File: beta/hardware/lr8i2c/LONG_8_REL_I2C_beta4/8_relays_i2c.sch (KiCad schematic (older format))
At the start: 86 parts, among them K101 G5LA-1-12VDC, K102 G5LA-1-12VDC, K103 G5LA-1-12VDC, K104 G5LA-1-12VDC, K105 G5LA-1-12VDC, K106 G5LA-1-12VDC, K107 G5LA-1-12VDC, K108 G5LA-1-12VDC, P101 CONN_3, P102 CONN_3, P103 CONN_3, P104 CONN_3, P105 CONN_3, P106 CONN_3, P107 CONN_3, P108 CONN_3, P109 CONN_2, P110 CONN_6, P112 CONN_6, Q101 PNP, Q102 PNP, Q103 PNP, Q104 PNP, Q105 PNP, Q106 PNP, Q107 PNP, Q108 PNP, Q109 DSS20201L NPN, Q110 DSS20201L NPN, Q111 DSS20201L NPN, Q112 DSS20201L NPN, Q113 DSS20201L NPN, Q114 DSS20201L NPN, Q115 DSS20201L NPN, Q116 DSS20201L NPN, U101 PCF8574P

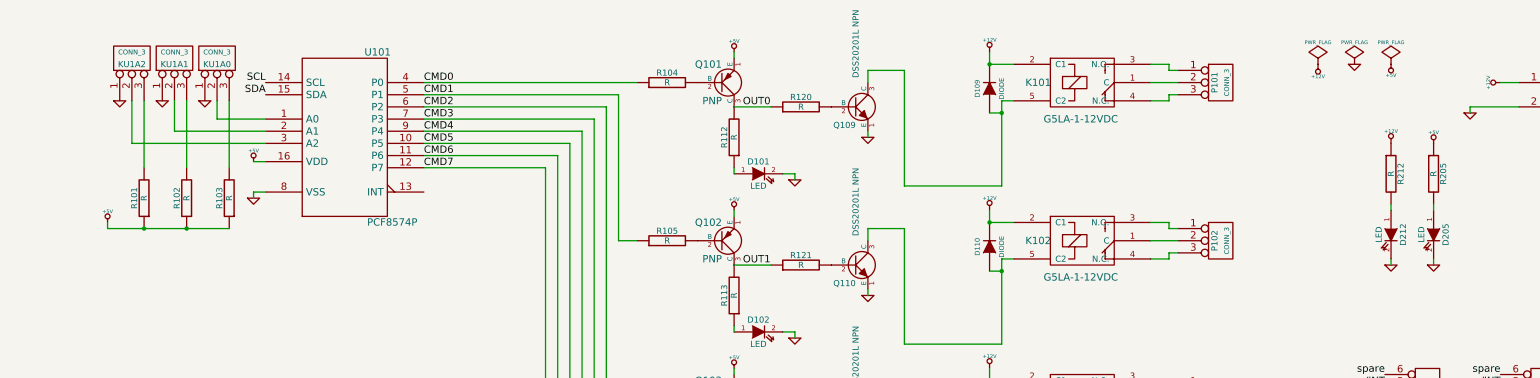
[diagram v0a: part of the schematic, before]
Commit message: Suppression 2 des 3 resistances de pull-up d'adressage Ajout pre-disposition 2 resistance de pull-up SDA/SCL Controle DRC ok
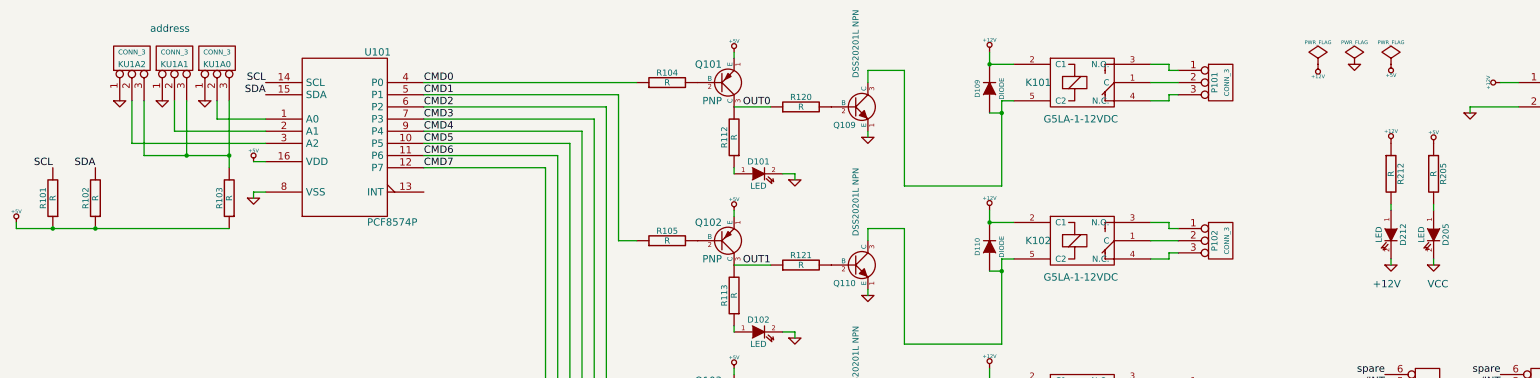
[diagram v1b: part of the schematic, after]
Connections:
- net SCL: now also R101.2
- net SDA: now also R102.2
- net at KU1A2.3 (P3): now also KU1A0.3 (P3), KU1A1.3 (P3), R103.2; no longer R101.2
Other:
- note added: "+12V"
- note added: "VCC"
- note added: "address"
- moved on the sheet: R101, R102

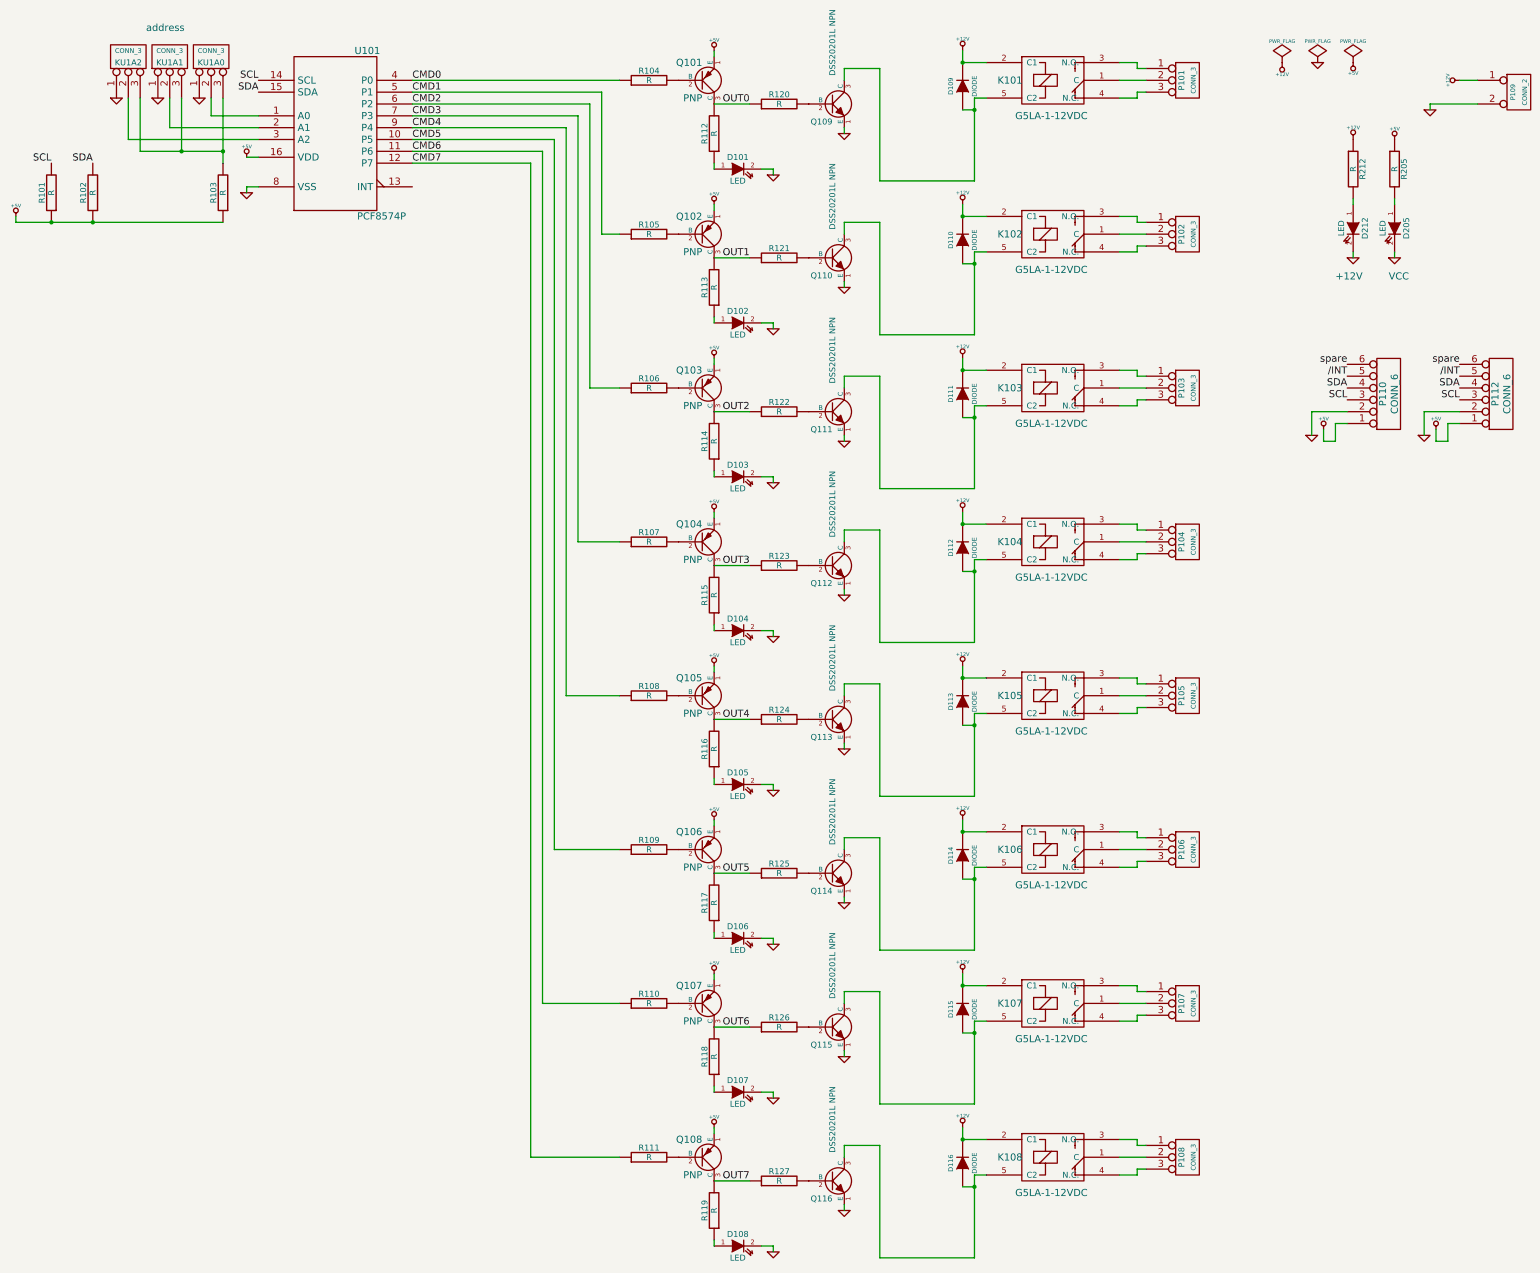
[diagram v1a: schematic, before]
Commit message: ajout d'un second connecteur GND-12V ajout logos DRC ok
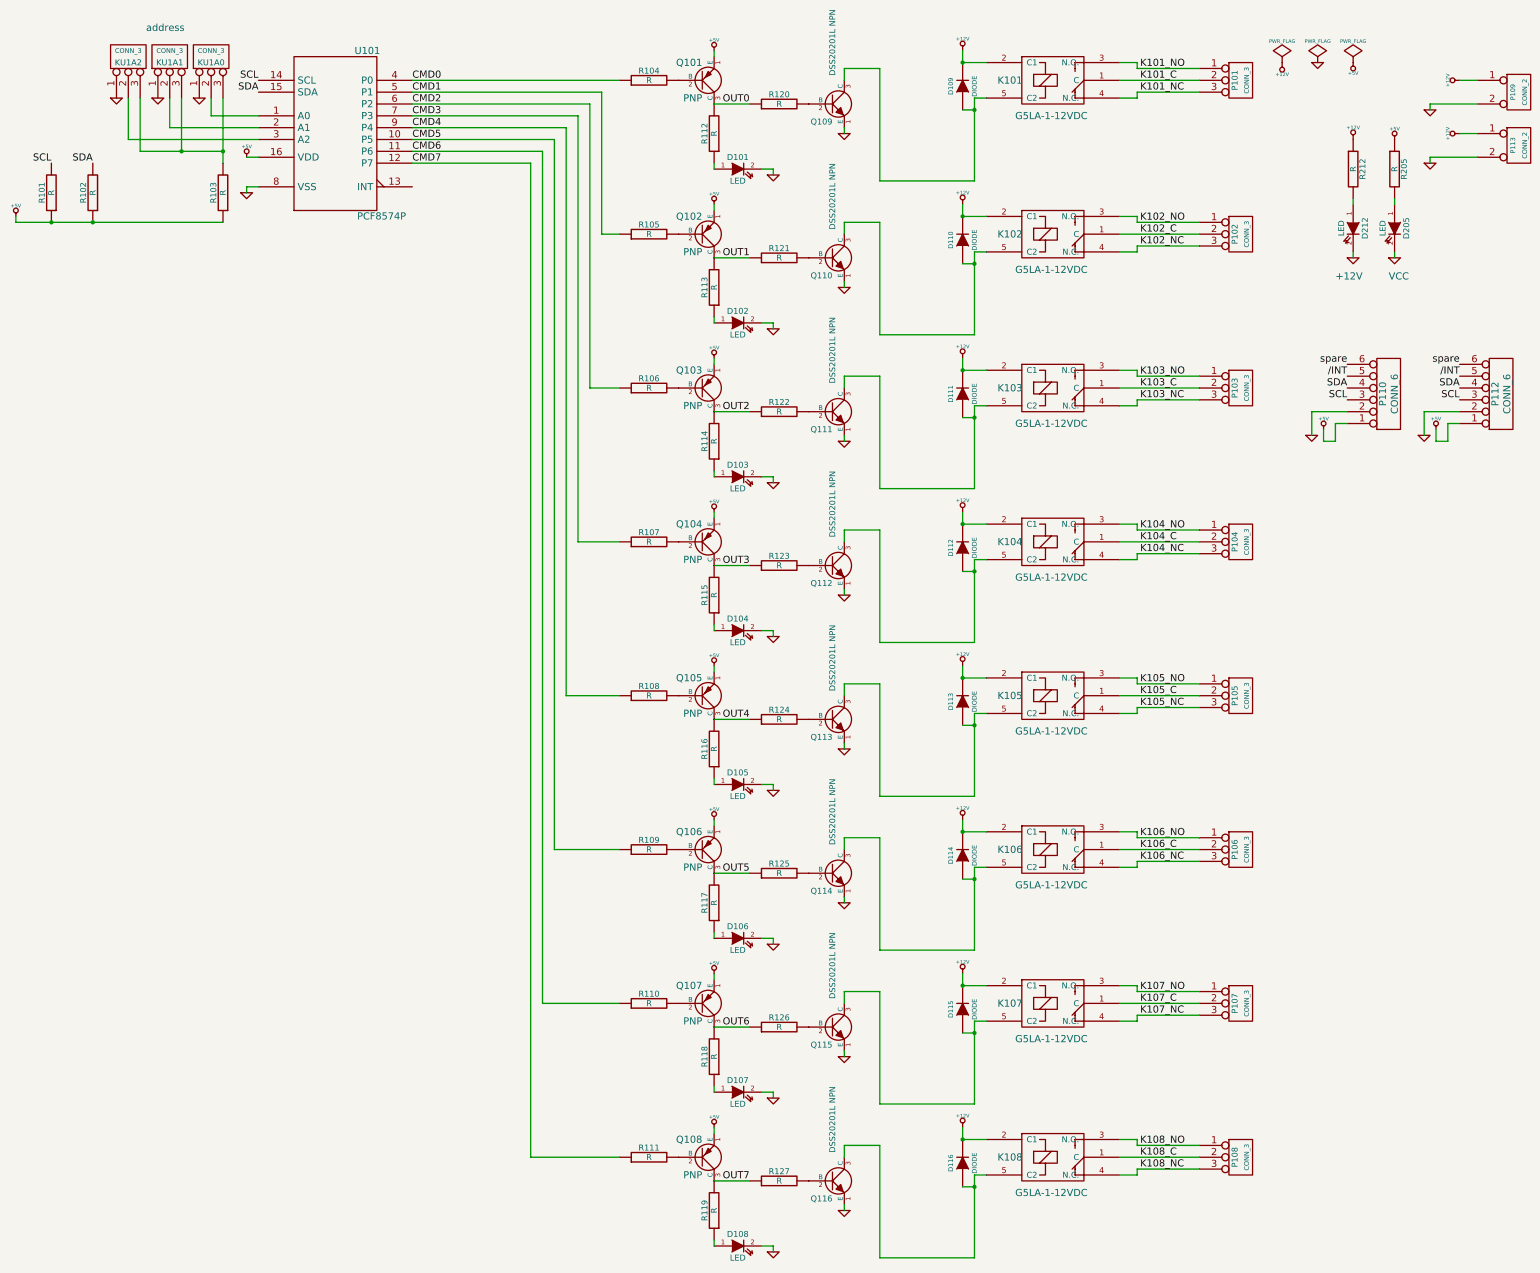
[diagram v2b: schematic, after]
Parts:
- added P113: CONN_2, symbol CONN_2
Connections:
- net +12V: now also P113.1 (P1)
- net GND: now also P113.2 (PM)
- net K101_C: now reaches K101.1 (C), P101.2 (PM)
- net K101_NO: now reaches K101.3 (N.O.), P101.1 (P1)
- net K101_NC: now reaches K101.4 (N.C.), P101.3 (P3)
- net K102_NO: now reaches K102.3 (N.O.), P102.1 (P1)
- net K102_C: now reaches K102.1 (C), P102.2 (PM)
- net K102_NC: now reaches K102.4 (N.C.), P102.3 (P3)
- net K104_C: now reaches K104.1 (C), P104.2 (PM)
- net K104_NO: now reaches K104.3 (N.O.), P104.1 (P1)
- net K104_NC: now reaches K104.4 (N.C.), P104.3 (P3)
- net K103_NO: now reaches K103.3 (N.O.), P103.1 (P1)
- net K103_C: now reaches K103.1 (C), P103.2 (PM)
- net K103_NC: now reaches K103.4 (N.C.), P103.3 (P3)
- net K107_C: now reaches K107.1 (C), P107.2 (PM)
- net K107_NO: now reaches K107.3 (N.O.), P107.1 (P1)
- net K107_NC: now reaches K107.4 (N.C.), P107.3 (P3)
- net K108_NO: now reaches K108.3 (N.O.), P108.1 (P1)
- net K108_C: now reaches K108.1 (C), P108.2 (PM)
- net K108_NC: now reaches K108.4 (N.C.), P108.3 (P3)
- net K106_C: now reaches K106.1 (C), P106.2 (PM)
- net K106_NO: now reaches K106.3 (N.O.), P106.1 (P1)
- net K106_NC: now reaches K106.4 (N.C.), P106.3 (P3)
- net K105_NO: now reaches K105.3 (N.O.), P105.1 (P1)
- net K105_C: now reaches K105.1 (C), P105.2 (PM)
- net K105_NC: now reaches K105.4 (N.C.), P105.3 (P3)
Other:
- moved on the sheet: P101, P102, P103, P104, P105, P106, P107, P108
